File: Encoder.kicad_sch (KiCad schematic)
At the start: 20 parts, among them J4 Conn_01x05, J7 Conn_01x05, U5 AS5047D

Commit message: more layout
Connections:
- net QUAD_ENC_A: now also D1.4 (I/O); no longer D1.6 (I/O)
- net QUAD_ENC_B: now also D1.6 (I/O); no longer D1.4 (I/O)
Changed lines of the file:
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@@
 	)
 	(junction
-		(at 76.2 104.14)
+		(at 86.36 104.14)
 		(diameter 0)
 		(color 0 0 0 0)
@@
 	)
 	(junction
-		(at 86.36 106.68)
-		(diameter 0)
-		(color 0 0 0 0)
-	)
-	(junction
 		(at 140.97 31.75)
 		(diameter 0)
@@
 		(color 0 0 0 0)
 	)
+	(junction
+		(at 76.2 106.68)
+		(diameter 0)
+		(color 0 0 0 0)
+	)
 	(wire
 		(pts
@@
 	(wire
 		(pts
-			(xy 60.96 104.14) (xy 76.2 104.14)
+			(xy 60.96 104.14) (xy 86.36 104.14)
 		)
 		(stroke
@@
 	(wire
 		(pts
+			(xy 76.2 106.68) (xy 76.2 124.46)
+		)
+		(stroke
+			(width 0)
+			(type default)
+		)
+	)
+	(wire
+		(pts
 			(xy 140.97 31.75) (xy 140.97 48.26)
 		)
@@
 	(wire
 		(pts
+			(xy 76.2 106.68) (xy 90.17 106.68)
+		)
+		(stroke
+			(width 0)
+			(type default)
+		)
+	)
+	(wire
+		(pts
 			(xy 120.65 58.42) (xy 128.27 58.42)
 		)
@@
 	(wire
 		(pts
-			(xy 76.2 104.14) (xy 106.68 104.14)
+			(xy 86.36 104.14) (xy 106.68 104.14)
 		)
 		(stroke
@@
 	(wire
 		(pts
-			(xy 86.36 106.68) (xy 86.36 124.46)
-		)
-		(stroke
-			(width 0)
-			(type default)
-		)
-	)
-	(wire
-		(pts
 			(xy 76.2 149.86) (xy 76.2 166.37)
 		)
@@
 	(wire
 		(pts
-			(xy 90.17 106.68) (xy 86.36 106.68)
+			(xy 60.96 106.68) (xy 76.2 106.68)
 		)
 		(stroke
@@
 	(wire
 		(pts
-			(xy 86.36 106.68) (xy 60.96 106.68)
-		)
-		(stroke
-			(width 0)
-			(type default)
-		)
-	)
-	(wire
-		(pts
 			(xy 50.8 173.99) (xy 50.8 171.45)
 		)
@@
 	(wire
 		(pts
+			(xy 86.36 104.14) (xy 86.36 124.46)
+		)
+		(stroke
+			(width 0)
+			(type default)
+		)
+	)
+	(wire
+		(pts
 			(xy 60.96 166.37) (xy 76.2 166.37)
 		)
@@
 		)
 		(stroke
-			(width 0)
-			(type default)
-		)
-	)
-	(wire
-		(pts
-			(xy 76.2 104.14) (xy 76.2 124.46)
-		)
-		(stroke

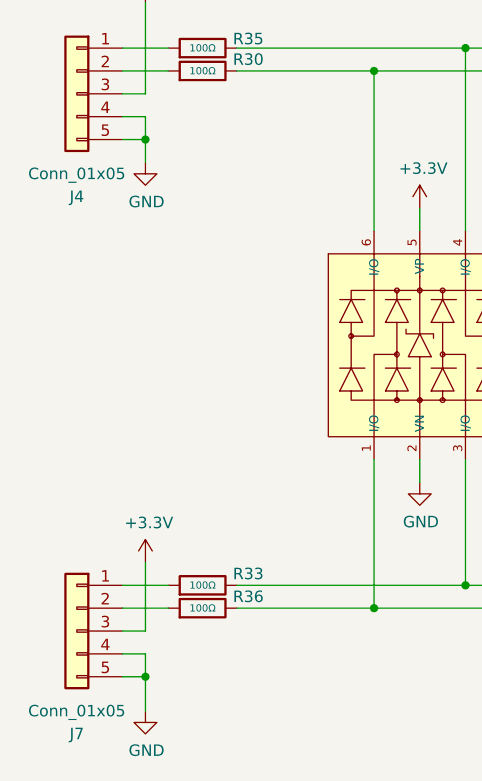
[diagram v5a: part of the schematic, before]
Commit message: Finished layout, pcba is being tested
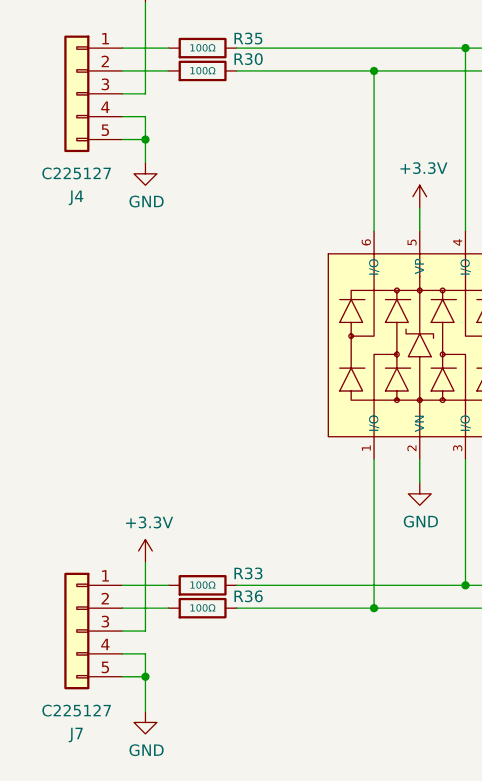
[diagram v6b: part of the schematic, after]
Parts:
- J4, J7: value Conn_01x05 -> C225127
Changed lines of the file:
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@@
 			)
 		)
-		(property "Value" "Conn_01x05"
+		(property "Value" "C225127"
 			(at 43.18 177.8 0)
 			(effects
@@
 			)
 		)
-		(property "Value" "Conn_01x05"
+		(property "Value" "C225127"
 			(at 43.18 118.11 0)
 			(effects
